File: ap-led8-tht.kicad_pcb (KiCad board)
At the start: 2 copper layers, 10 parts, among them J1 Conn_01x08_Socket, J2 Conn_01x08_Socket

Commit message: Initial PCB
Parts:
- moved D1 90.4 mm to (110.5, 54.6)
- moved D0 90.4 mm to (115.6, 54.6)
- moved D2 90.4 mm to (105.4, 54.6)
- moved D4 90.4 mm to (95.2, 54.6)
- moved D6 90.4 mm to (85.1, 54.6)
- moved D3 90.4 mm to (100.3, 54.6)
- moved D5 90.4 mm to (90.2, 54.6)
- moved D7 90.4 mm to (80.0, 54.6)
- moved J1 90.4 mm to (80.0, 63.5)
- moved J2 90.4 mm to (80.0, 58.4)
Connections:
- D0 pad 2: unconnected-(D0-A-Pad2) -> /led0
- D1 pad 2: unconnected-(D1-A-Pad2) -> /led1
- D2 pad 2: unconnected-(D2-A-Pad2) -> /led2
- D3 pad 2: unconnected-(D3-A-Pad2) -> /led3
- D4 pad 2: unconnected-(D4-A-Pad2) -> /led4
- D5 pad 2: unconnected-(D5-A-Pad2) -> /led5
- J1 pad 3: unconnected-(J1-Pin_3-Pad3) -> /led5
- J1 pad 4: unconnected-(J1-Pin_4-Pad4) -> /led4
- J1 pad 5: unconnected-(J1-Pin_5-Pad5) -> /led3
- J1 pad 6: unconnected-(J1-Pin_6-Pad6) -> /led2
- J1 pad 7: unconnected-(J1-Pin_7-Pad7) -> /led1
- J1 pad 8: unconnected-(J1-Pin_8-Pad8) -> /led0
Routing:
- net GND: track 0.00 -> 53.1 mm
- net /led0: track 0.00 -> 22.5 mm
- net /led1: track 0.00 -> 20.6 mm
- net /led2: track 0.00 -> 20.3 mm
- net /led3: track 0.00 -> 17.6 mm
- net /led4: track 0.00 -> 15.0 mm
- net /led5: track 0.00 -> 13.5 mm
- net /led6: track 0.00 -> 12.5 mm
- net /led7: track 0.00 -> 12.5 mm
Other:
- board outline added: 40 x 15.9 mm

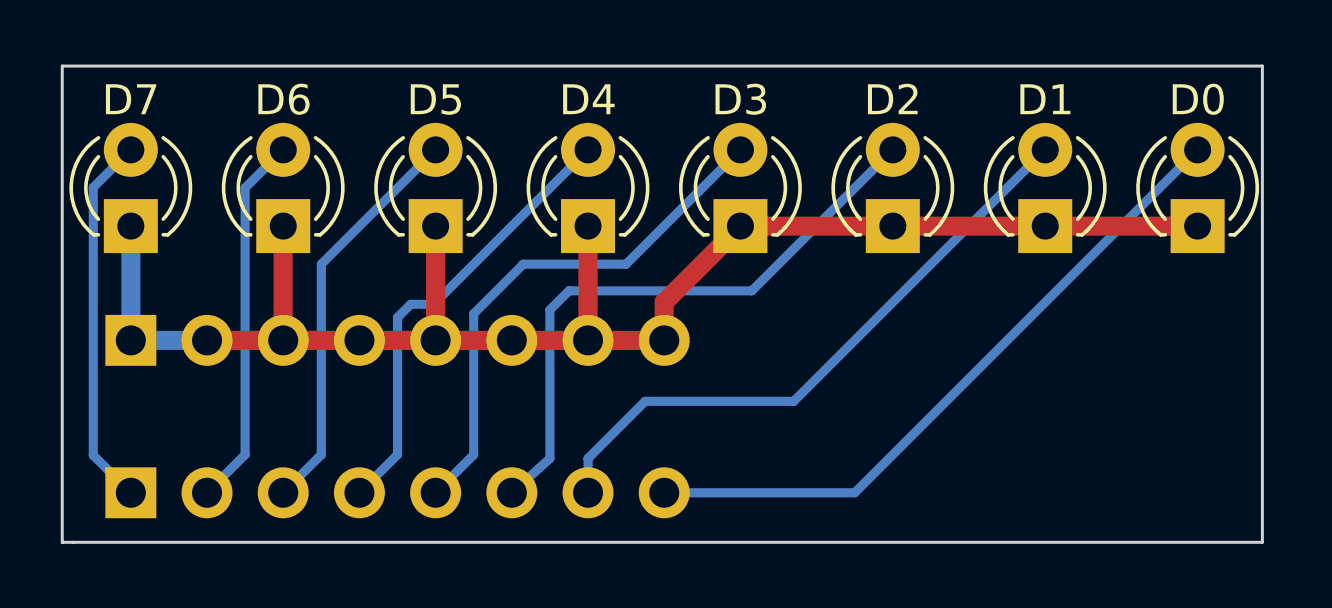
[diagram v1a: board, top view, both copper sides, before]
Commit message: add top and bottom silkscreens
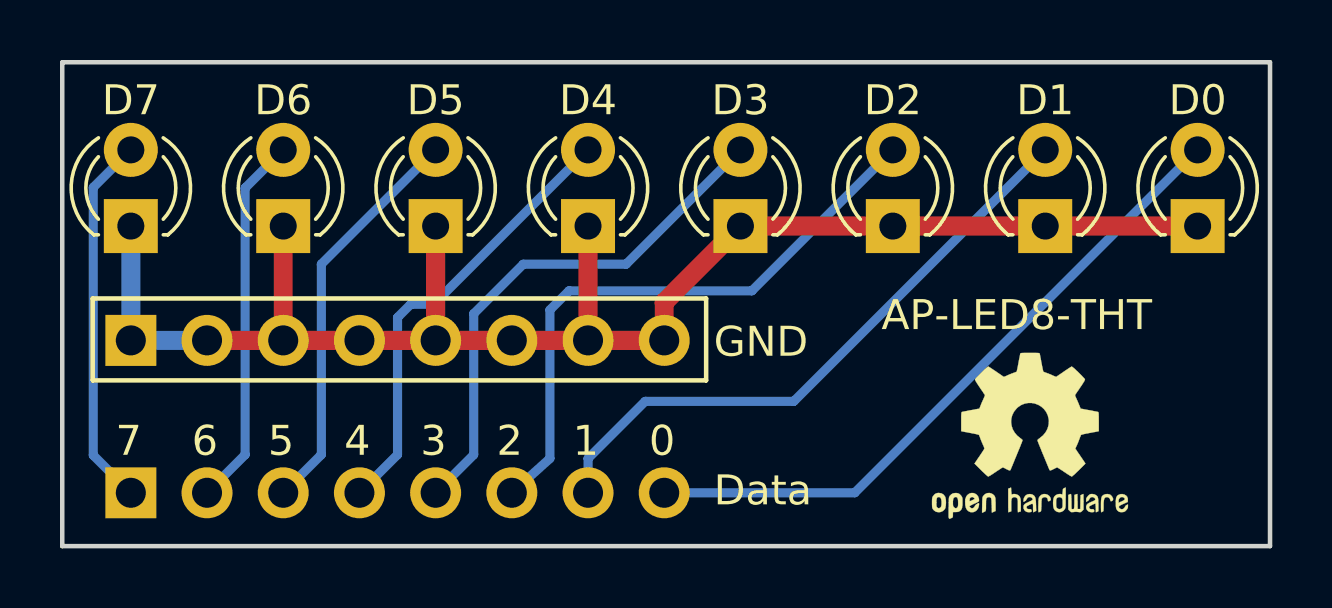
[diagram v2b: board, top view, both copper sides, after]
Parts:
- added REF**: OSHW-Logo2_7.3x6mm_SilkScreen, Symbol:OSHW-Logo2_7.3x6mm_SilkScreen, F.Cu at (110.0, 61.6)
- added REF**: KiCad-Logo2_5mm_SilkScreen, Symbol:KiCad-Logo2_5mm_SilkScreen, B.Cu at (111.0, 61.5)
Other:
- board size 40 x 15.9 mm -> 40.3 x 16.1 mm
- board text added: "0"
- board text added: "1"
- board text added: "2"
- board text added: "3"
- board text added: "4"
- board text added: "5"
- board text added: "6"
- board text added: "7"
- board text added: "AP-LED8-THT"
- board text added: "D0"
- board text added: "D1"
- board text added: "D2"
- board text added: "D3"
- board text added: "D4"
- board text added: "D5"
- board text added: "D6"
- board text added: "D7"
- board text added: "Data"
- board text added: "GND"

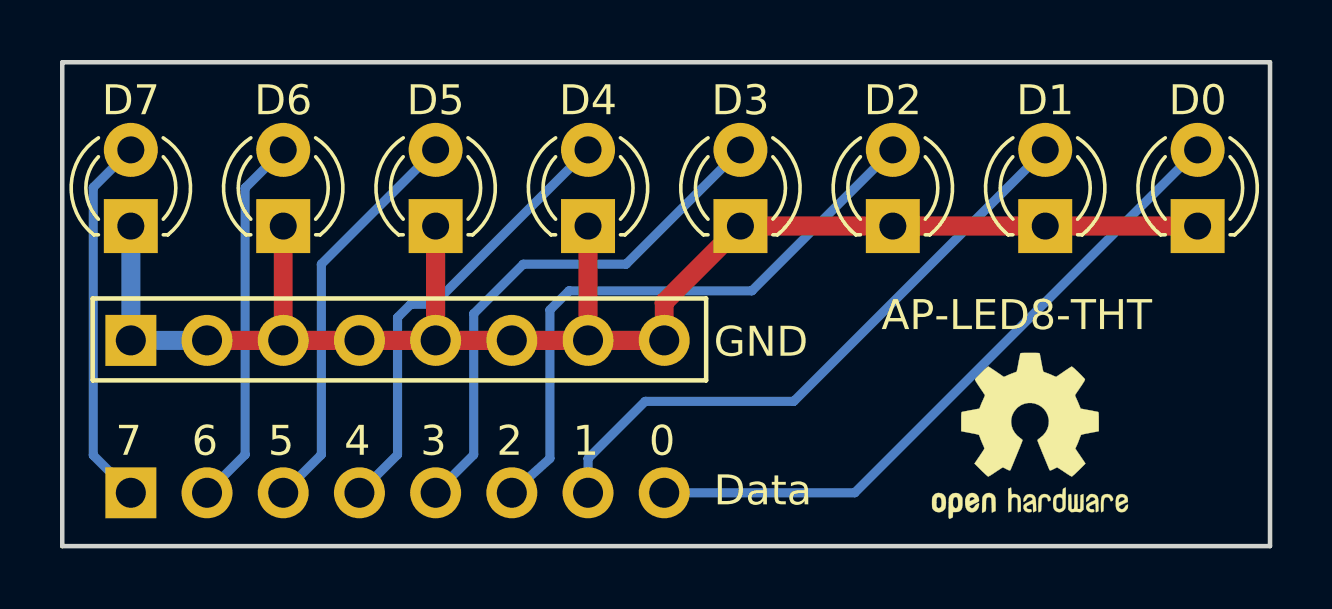
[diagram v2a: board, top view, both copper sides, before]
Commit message: LEDs moved to make the board less in width
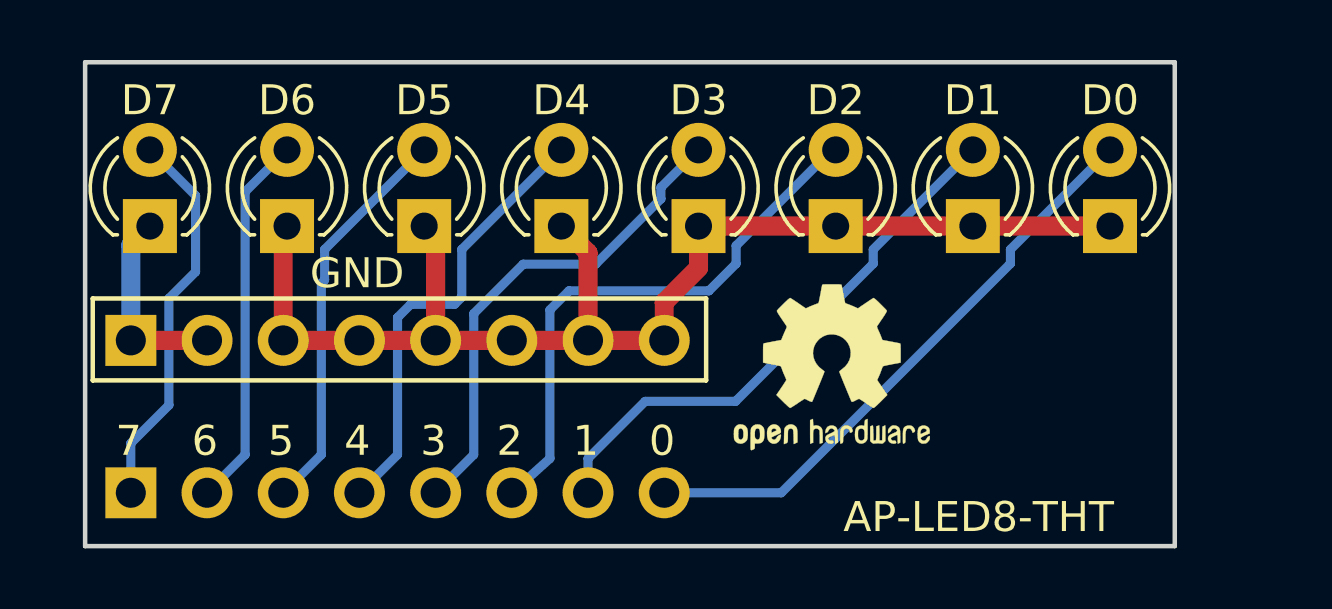
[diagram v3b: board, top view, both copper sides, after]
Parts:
- moved REF** 6.99 mm to (103.4, 59.3)
- moved REF** 3.18 mm to (107.8, 61.5)
- moved D0 2.92 mm to (112.6, 54.6)
- moved D1 2.41 mm to (108.1, 54.6)
- moved D2 1.91 mm to (103.5, 54.6)
- moved D3 1.40 mm to (98.9, 54.6)
- moved D4 0.89 mm to (94.4, 54.6)
- moved D7 0.63 mm to (80.6, 54.6)
- moved D5 0.38 mm to (89.8, 54.6)
- moved D6 0.13 mm to (85.2, 54.6)
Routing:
- net GND: track 53.1 -> 49.3 mm
- net /led0: track 22.5 -> 19.9 mm
- net /led1: track 20.6 -> 18.5 mm
- net /led2: track 20.3 -> 18.7 mm
- net /led3: track 17.6 -> 16.8 mm
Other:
- board size 40.3 x 16.1 mm -> 36.3 x 16.1 mm
- board text removed: "Data"

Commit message: pcb: update silkscreen
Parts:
- removed the REF** at (103.4, 59.3)
- added REF**: OSHW-Logo_5.7x6mm_SilkScreen, Symbol:OSHW-Logo_5.7x6mm_SilkScreen, F.Cu at (101.9, 59.3)
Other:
- board text added: "@obijuan_cube"

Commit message: pcb: update silkscreen
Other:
- board text added: "Certification"
- board text added: "Mark"
- board text added: "TODO: OSHW"
